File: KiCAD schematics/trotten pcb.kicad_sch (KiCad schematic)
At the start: 21 parts, among them J1 Conn_01x04_Socket, J2 Conn_01x05_Socket, J3 Conn_01x05_Socket, J4 Conn_01x04_Socket, J5 Conn_02x03_Odd_Even, M1 Motor_DC, SW1 Haut, SW2 Bas, SW3 MEM_1, SW4 MEM_2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

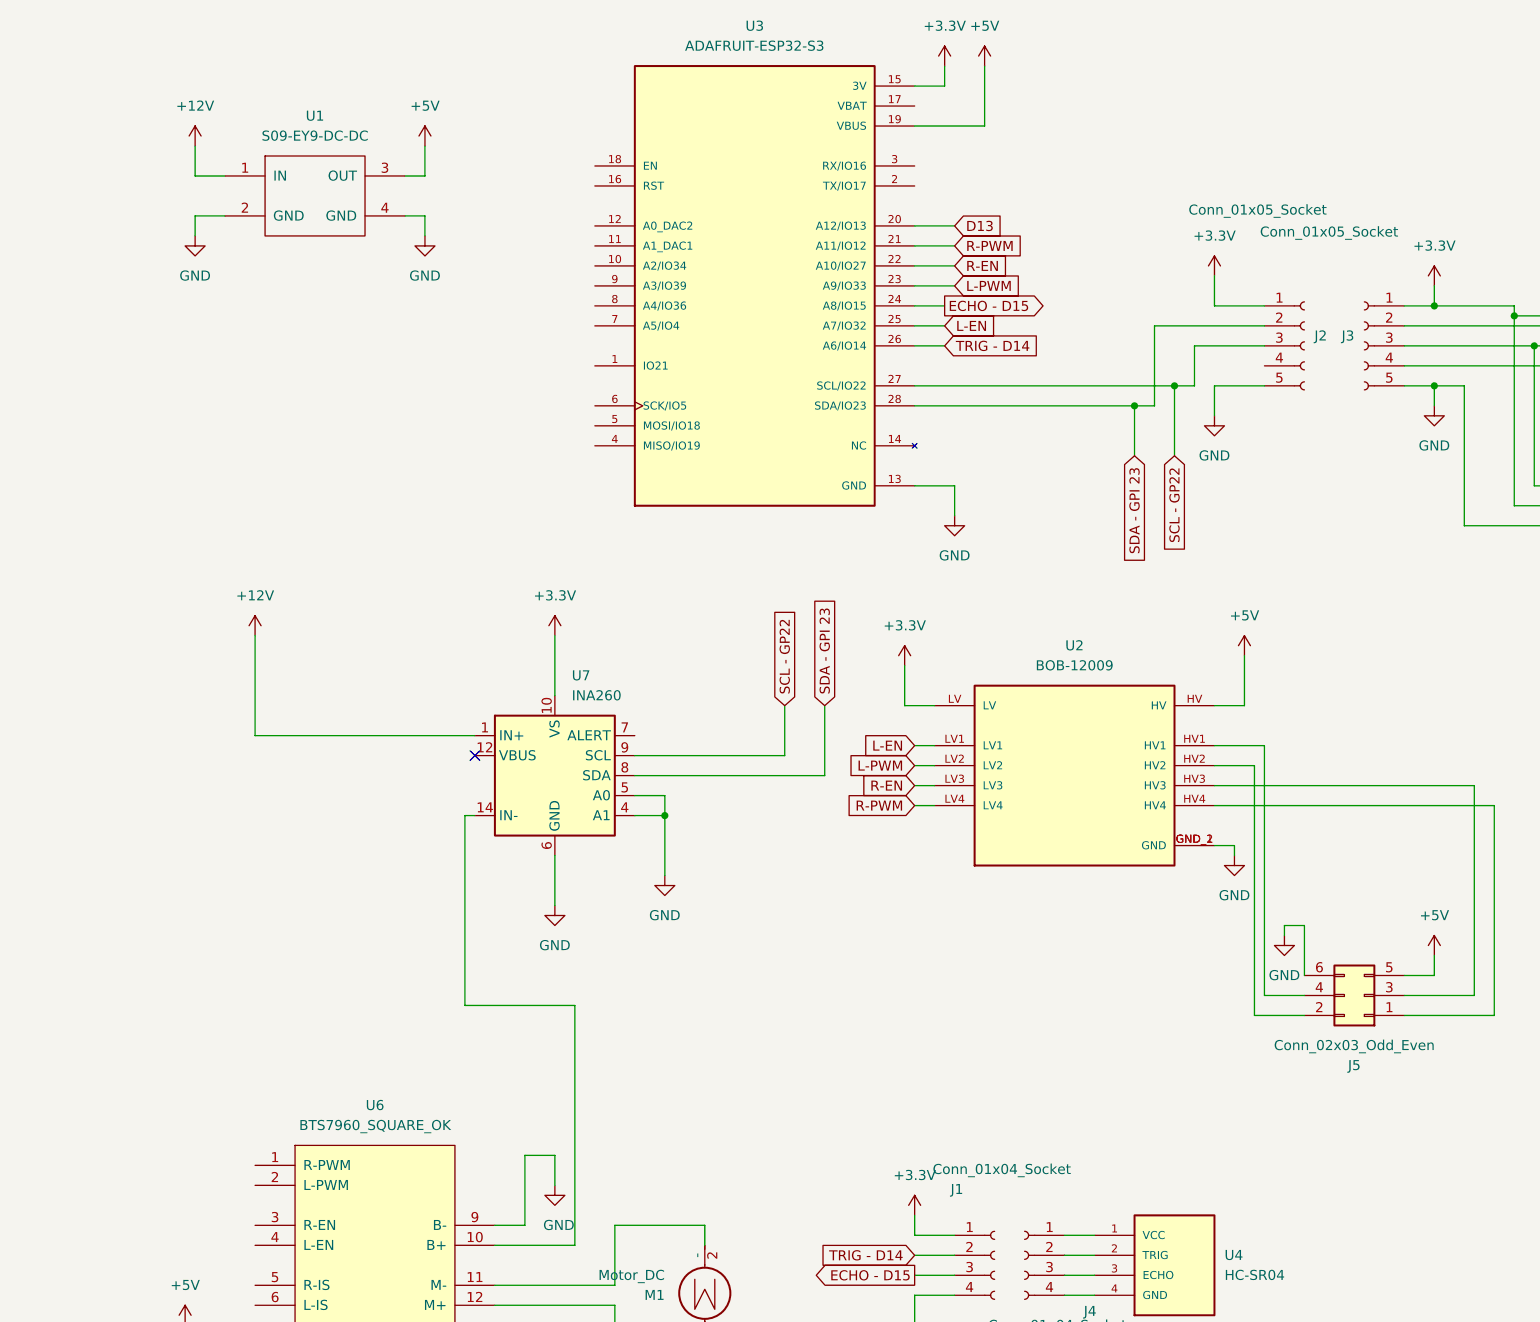
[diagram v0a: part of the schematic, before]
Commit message: SSD1306 working on esp32 s3
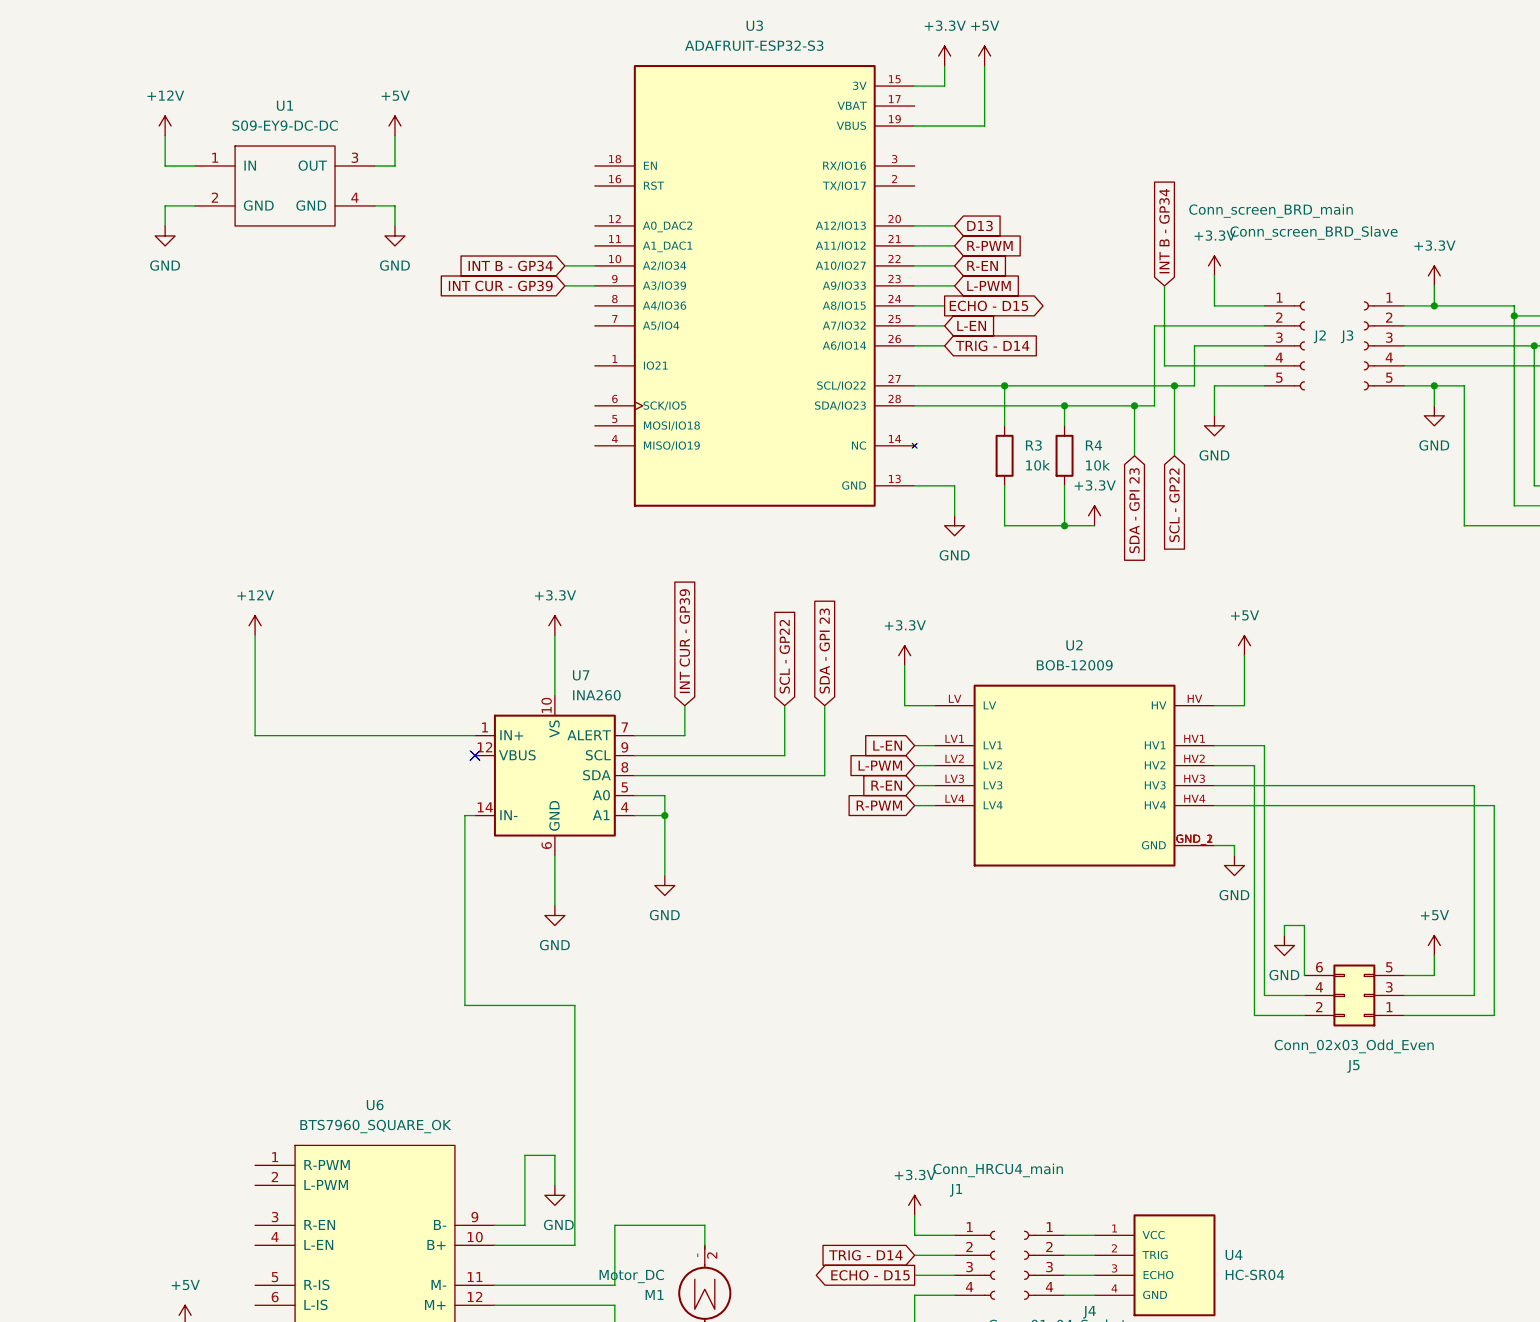
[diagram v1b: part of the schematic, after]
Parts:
- added R3, R4: 10k, Resistor_THT:R_Axial_DIN0207_L6.3mm_D2.5mm_P7.62mm_Horizontal, symbol Device:R
- J1: value Conn_01x04_Socket -> Conn_HRCU4_main
- J2: value Conn_01x05_Socket -> Conn_screen_BRD_main
- J3: value Conn_01x05_Socket -> Conn_screen_BRD_Slave
- R1, R2: footprint (none) -> Resistor_THT:R_Axial_DIN0207_L6.3mm_D2.5mm_P7.62mm_Horizontal
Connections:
- net +3.3V: now also R3.2, R4.2
- net SCL - GP22: now also R3.1
- net SDA - GPI 23: now also R4.1
- net INT B - GP34: now reaches J2.4 (Pin_4)
- net INT B - GP34: now also U3.10 (A2/IO34)
- net INT CUR - GP39: now reaches U7.7 (ALERT)
- net INT CUR - GP39: now also U3.9 (A3/IO39)
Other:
- moved on the sheet: U1

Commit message: avancement PCB et 3d files
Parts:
- removed SW5: MEM_3, symbol Switch:SW_Push
- Brd1: footprint (none) -> SSD1306:SSD1306
- MODULE1: footprint CJMCU-2317 MCP23017 I2C SERIAL INTERFACE 16 BIT I:O EXPANDER SERIAL MODULE -> Adafruit_23017:MCP23017_ADAFRUIT
- SW1, SW2, SW3, SW4: footprint (none) -> Button_6_6:6x6x5_Button
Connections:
- net at Brd1.4 (SDA), J3.2 (Pin_2): now also MODULE1.27 (SDA/SI), R2.2
- net at Brd1.3 (SCL), J3.3 (Pin_3): now also MODULE1.28 (SCL/SCK), R1.2
- no-connect marks 19 -> 20
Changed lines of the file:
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@@
 	)
 	(junction
-		(at 187.96 55.88)
+		(at 257.81 39.37)
 		(diameter 0)
 		(color 0 0 0 0)
@@
 	)
 	(junction
-		(at 278.13 104.14)
+		(at 250.19 20.32)
 		(diameter 0)
 		(color 0 0 0 0)
 	)
 	(junction
-		(at 250.19 20.32)
+		(at 278.13 80.01)
 		(diameter 0)
 		(color 0 0 0 0)
 	)
 	(junction
-		(at 278.13 80.01)
+		(at 130.81 67.31)
 		(diameter 0)
 		(color 0 0 0 0)
 	)
 	(junction
-		(at 130.81 67.31)
+		(at 250.19 36.83)
 		(diameter 0)
 		(color 0 0 0 0)
@@
 	)
 	(junction
+		(at 187.96 54.61)
+		(diameter 0)
+		(color 0 0 0 0)
+	)
+	(junction
 		(at 139.7 67.31)
 		(diameter 0)
@@
 		(at 212.09 54.61)
 	)
+	(no_connect
+		(at 242.57 67.31)
+	)
 	(wire
 		(pts
@@
 	(wire
 		(pts
-			(xy 190.5 59.69) (xy 200.66 59.69)
+			(xy 190.5 59.69) (xy 199.39 59.69)
 		)
 		(stroke
@@
 	(wire
 		(pts
-			(xy 267.97 104.14) (xy 278.13 104.14)
+			(xy 66.04 162.56) (xy 66.04 166.37)
 		)
 		(stroke
@@
 	(wire
 		(pts
-			(xy 66.04 162.56) (xy 66.04 166.37)
+			(xy 187.96 54.61) (xy 177.8 54.61)
 		)
 		(stroke
@@
 	(wire
 		(pts
-			(xy 187.96 54.61) (xy 177.8 54.61)
+			(xy 269.24 36.83) (xy 250.19 36.83)
 		)
 		(stroke
@@
 	(wire
 		(pts
-			(xy 191.77 20.32) (xy 191.77 55.88)
+			(xy 269.24 16.51) (xy 269.24 36.83)
 		)
 		(stroke
@@
 	(wire
 		(pts
-			(xy 242.57 34.29) (xy 278.13 34.29)
+			(xy 191.77 20.32) (xy 191.77 54.61)
 		)
 		(stroke
@@
 	(wire
 		(pts
-			(xy 255.27 68.58) (xy 257.81 68.58)
+			(xy 242.57 34.29) (xy 278.13 34.29)
 		)
 		(stroke
@@
 	(wire
 		(pts
-			(xy 242.57 59.69) (xy 255.27 59.69)
+			(xy 255.27 68.58) (xy 257.81 68.58)
 		)
 		(stroke
@@
 	(wire
 		(pts
-			(xy 278.13 92.71) (xy 278.13 104.14)
+			(xy 242.57 59.69) (xy 255.27 59.69)
 		)
 		(stroke
@@
 	(wire
 		(pts
-			(xy 182.88 115.57) (xy 182.88 142.24)
+			(xy 278.13 92.71) (xy 278.13 111.76)
 		)
 		(stroke
@@
 	(wire
 		(pts
-			(xy 45.72 33.02) (xy 45.72 36.83)
+			(xy 182.88 115.57) (xy 182.88 142.24)
 		)
 		(stroke
@@
 	(wire
 		(pts
-			(xy 196.85 57.15) (xy 196.85 48.26)
+			(xy 45.72 33.02) (xy 45.72 36.83)
 		)
 		(stroke
@@
 	(wire
 		(pts
-			(xy 187.96 55.88) (xy 187.96 54.61)
-		)
-		(stroke
-			(width 0)
-			(type default)
-		)
-	)
-	(wire
-		(pts
 			(xy 116.84 77.47) (xy 116.84 81.28)
 		)
@@
 	(wire
 		(pts
-			(xy 191.77 55.88) (xy 187.96 55.88)
+			(xy 191.77 54.61) (xy 187.96 54.61)
 		)
 		(stroke
@@
 	(wire
 		(pts
+			(xy 187.96 54.61) (xy 187.96 80.01)
+		)
+		(stroke
+			(width 0)
+			(type default)
+		)
+	)
+	(wire
+		(pts
 			(xy 149.86 54.61) (xy 156.21 54.61)
 		)
@@
 	(wire
 		(pts
+			(xy 196.85 15.24) (xy 196.85 57.15)
+		)
+		(stroke
+			(width 0)
+			(type default)
+		)
+	)
+	(wire
+		(pts
 			(xy 111.76 52.07) (xy 116.84 52.07)
 		)
@@
 	(wire
 		(pts
+			(xy 199.39 16.51) (xy 269.24 16.51)
+		)
+		(stroke
+			(width 0)
+			(type default)
+		)
+	)
+	(wire
+		(pts
 			(xy 257.81 80.01) (xy 252.73 80.01)
 		)
@@
 	(wire
 		(pts
+			(xy 270.51 15.24) (xy 270.51 39.37)
+		)
+		(stroke
+			(width 0)
+			(type default)
+		)
+	)
+	(wire
+		(pts
 			(xy 120.65 24.13) (xy 120.65 31.75)
 		)
@@
 	(wire
 		(pts
-			(xy 187.96 80.01) (xy 187.96 55.88)
-		)
-		(stroke
-			(width 0)
-			(type default)
-		)
-	)
-	(wire
-		(pts
 			(xy 76.2 109.22) (xy 82.55 109.22)
 		)
@@
 	(wire
 		(pts
-			(xy 247.65 104.14) (xy 257.81 104.14)
-		)
-		(stroke
-			(width 0)
-			(type default)
-		)
-	)
-	(wire
-		(pts
 			(xy 111.76 175.26) (xy 116.84 175.26)
 		)
@@
 	(wire
 		(pts
+			(xy 199.39 59.69) (xy 199.39 16.51)
+		)
+		(stroke
+			(width 0)
+			(type default)
+		)
+	)
+	(wire
+		(pts
 			(xy 67.31 49.53) (xy 71.12 49.53)
 		)
@@
 	(wire
 		(pts
-			(xy 278.13 34.29) (xy 278.13 57.15)
+			(xy 196.85 15.24) (xy 270.51 15.24)
 		)
 		(stroke
@@
 	(wire
 		(pts
-			(xy 27.94 186.69) (xy 19.05 186.69)
+			(xy 270.51 39.37) (xy 257.81 39.37)
 		)
 		(stroke
@@
 	(wire
 		(pts
-			(xy 250.19 92.71) (xy 250.19 64.77)
+			(xy 278.13 34.29) (xy 278.13 57.15)
 		)
 		(stroke
@@
 	(wire
 		(pts
-			(xy 66.04 124.46) (xy 66.04 130.81)
+			(xy 27.94 186.69) (xy 19.05 186.69)
 		)
 		(stroke
@@
 	(wire
 		(pts
-			(xy 116.84 44.45) (xy 111.76 44.45)
+			(xy 250.19 92.71) (xy 250.19 64.77)
 		)
 		(stroke
@@
 	(wire
 		(pts
-			(xy 149.86 123.19) (xy 152.4 123.19)
+			(xy 66.04 124.46) (xy 66.04 130.81)
 		)
 		(stroke
@@
 	(wire
 		(pts
-			(xy 177.8 64.77) (xy 177.8 67.31)
+			(xy 116.84 44.45) (xy 111.76 44.45)
 		)
 		(stroke
@@
 	(wire
 		(pts
-			(xy 278.13 104.14) (xy 278.13 111.76)
+			(xy 149.86 123.19) (xy 152.4 123.19)
+		)
+		(stroke
+			(width 0)
+			(type default)
+		)
+	)
+	(wire
+		(pts
+			(xy 177.8 64.77) (xy 177.8 67.31)
 		)
 		(stroke
@@
 	(wire
 		(pts
-			(xy 200.66 48.26) (xy 200.66 59.69)
-		)
-		(stroke
-			(width 0)
-			(type default)
-		)
-	)
-	(wire
-		(pts
 			(xy 134.62 175.26) (xy 130.81 175.26)
 		)
@@
 	(wire
 		(pts
-			(xy 242.57 67.31) (xy 247.65 67.31)
-		)
-		(stroke
-			(width 0)
-			(type default)
-		)
-	)
-	(wire
-		(pts
 			(xy 191.77 20.32) (xy 246.38 20.32)
 		)
@@
 	(wire
 		(pts
-			(xy 247.65 67.31) (xy 247.65 104.14)
-		)
-		(stroke
-			(width 0)
-			(type default)
-		)
-	)
-	(wire
-		(pts
 			(xy 190.5 77.47) (xy 190.5 59.69)
 		)
@@
 			)
 		)
-		(property "Footprint" ""
+		(property "Footprint" "Button_6_6:6x6x5_Button"
 			(at 262.89 52.07 0)
 			(effects
@@
 			)
 		)
-		(property "Footprint" ""
+		(property "Footprint" "Button_6_6:6x6x5_Button"
 			(at 262.89 63.5 0)
 			(effects
@@
 	)
 	(symbol
-		(lib_id "Switch:SW_Push")
-		(at 262.89 104.14 0)
-		(unit 1)
-		(exclude_from_sim no)
-		(in_bom yes)
-		(on_board yes)
-		(dnp no)
-		(fields_autoplaced yes)
-		(property "Reference" "SW5"
-			(at 262.89 96.52 0)
-			(effects
-				(font
-					(size 1.27 1.27)
-				)
-			)
-		)
-		(property "Value" "MEM_3"
-			(at 262.89 99.06 0)
-			(effects
-				(font
-					(size 1.27 1.27)
-				)
-			)
-		)
-		(property "Footprint" ""
-			(at 262.89 99.06 0)
-			(effects
-				(font
-					(size 1.27 1.27)
-				)
-				(hide yes)
-			)
-		)
-		(property "Datasheet" "~"
-			(at 262.89 99.06 0)
-			(effects
-				(font
-					(size 1.27 1.27)
-				)
-				(hide yes)
-			)
-		)
-		(property "Description" "Push button switch, generic, two pins"
-			(at 262.89 104.14 0)
-			(effects
-				(font
-					(size 1.27 1.27)
-				)
-				(hide yes)
-			)
-		)
-		(pin "2"
-		)
-		(pin "1"
-		)
-		(instances
-			(project "trotten pcb"
-				(path "/615cbb6f-ee23-4ea9-8e98-9b9e34f836b3"
-					(reference "SW5")
-					(unit 1)
-				)
-			)
-		)
-	)
-	(symbol
 		(lib_id "power:GND")
 		(at 80.01 127 0)
@@
 			)
 		)
-		(property "Footprint" ""
+		(property "Footprint" "Button_6_6:6x6x5_Button"
 			(at 262.89 87.63 0)
 			(effects
@@
 			)
 		)
-		(property "Footprint" "CJMCU-2317 MCP23017 I2C SERIAL INTERFACE 16 BIT I:O EXPANDER SERIAL MODULE"
+		(property "Footprint" "Adafruit_23017:MCP23017_ADAFRUIT"
 			(at 227.33 30.48 0)
 			(effects
@@
 			)
 		)
-		(property "Footprint" ""
+		(property "Footprint" "SSD1306:SSD1306"
 			(at 195.58 78.74 0)
 			(effects
@@
 			)
 		)
-		(property "Footprint" ""
+		(property "Footprint" "Button_6_6:6x6x5_Button"
 			(at 262.89 74.93 0)
 			(effects
